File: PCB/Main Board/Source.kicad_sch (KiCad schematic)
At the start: 43 parts, among them K1 G2RL-1, U1 OPA1662

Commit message: minor
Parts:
- added JP? (x2): SolderJumper_2_Bridged, Jumper:SolderJumper-2_P1.3mm_Bridged_RoundedPad1.0x1.5mm, symbol Jumper:SolderJumper_2_Bridged
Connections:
- net Signal: now also JP?.1 (A)
- net at R?.1, U1.6 (-), U1.7: now also JP?.2 (B)
- net at R?.1, U?.1, U?.2 (-): now also JP?.2 (B)
- net at C?.1, JP1.2 (B), R?.2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: now also JP?.1 (A)
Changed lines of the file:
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@@
 	)
 	(junction
+		(at 31.75 104.14)
+		(diameter 0)
+		(color 0 0 0 0)
+	)
+	(junction
+		(at 82.55 53.34)
+		(diameter 0)
+		(color 0 0 0 0)
+	)
+	(junction
 		(at 55.88 101.6)
 		(diameter 0)
@@
 	(wire
 		(pts
+			(xy 31.75 104.14) (xy 36.83 104.14)
+		)
+		(stroke
+			(width 0)
+			(type default)
+		)
+	)
+	(wire
+		(pts
 			(xy 160.02 88.9) (xy 165.1 88.9)
 		)
@@
 	(wire
 		(pts
-			(xy 184.15 133.35) (xy 222.25 133.35)
+			(xy 182.88 133.35) (xy 222.25 133.35)
 		)
 		(stroke
@@
 	(wire
 		(pts
+			(xy 48.26 113.03) (xy 55.88 113.03)
+		)
+		(stroke
+			(width 0)
+			(type default)
+		)
+	)
+	(wire
+		(pts
 			(xy 101.6 140.97) (xy 114.3 140.97)
 		)
@@
 	(wire
 		(pts
-			(xy 31.75 104.14) (xy 36.83 104.14)
+			(xy 29.21 104.14) (xy 31.75 104.14)
 		)
 		(stroke
@@
 	(wire
 		(pts
+			(xy 107.95 62.23) (xy 107.95 50.8)
+		)
+		(stroke
+			(width 0)
+			(type default)
+		)
+	)
+	(wire
+		(pts
 			(xy 241.3 101.6) (xy 250.19 101.6)
 		)
@@
 	(wire
 		(pts
-			(xy 76.2 53.34) (xy 87.63 53.34)
+			(xy 76.2 53.34) (xy 82.55 53.34)
 		)
 		(stroke
@@
 	(wire
 		(pts
-			(xy 201.93 104.14) (xy 184.15 104.14)
+			(xy 100.33 62.23) (xy 107.95 62.23)
+		)
+		(stroke
+			(width 0)
+			(type default)
+		)
+	)
+	(wire
+		(pts
+			(xy 31.75 113.03) (xy 40.64 113.03)
+		)
+		(stroke
+			(width 0)
+			(type default)
+		)
+	)
+	(wire
+		(pts
+			(xy 201.93 104.14) (xy 182.88 104.14)
+		)
+		(stroke
+			(width 0)
+			(type default)
+		)
+	)
+	(wire
+		(pts
+			(xy 55.88 113.03) (xy 55.88 101.6)
 		)
 		(stroke
@@
 	(wire
 		(pts
+			(xy 31.75 113.03) (xy 31.75 104.14)
+		)
+		(stroke
+			(width 0)
+			(type default)
+		)
+	)
+	(wire
+		(pts
 			(xy 82.55 114.3) (xy 82.55 111.76)
 		)
@@
 	(wire
 		(pts
+			(xy 82.55 62.23) (xy 82.55 53.34)
+		)
+		(stroke
+			(width 0)
+			(type default)
+		)
+	)
+	(wire
+		(pts
 			(xy 82.55 48.26) (xy 87.63 48.26)
 		)
@@
 	(wire
 		(pts
+			(xy 92.71 62.23) (xy 82.55 62.23)
+		)
+		(stroke
+			(width 0)
+			(type default)
+		)
+	)
+	(wire
+		(pts
 			(xy 67.31 101.6) (xy 69.85 101.6)
 		)
@@
 	(wire
 		(pts
+			(xy 82.55 53.34) (xy 87.63 53.34)
+		)
+		(stroke
+			(width 0)
+			(type default)
+		)
+	)
+	(wire
+		(pts
 			(xy 66.04 43.18) (xy 63.5 43.18)
 		)
@@
 	(wire
 		(pts
-			(xy 184.15 104.14) (xy 184.15 133.35)
+			(xy 182.88 104.14) (xy 182.88 133.35)
 		)
 		(stroke
@@
 	(hierarchical_label "Signal"
 		(shape input)
-		(at 31.75 104.14 180)
+		(at 29.21 104.14 180)
 		(effects
 			(font
@@
 	)
 	(symbol
+		(lib_id "Jumper:SolderJumper_2_Bridged")
+		(at 44.45 113.03 0)
+		(unit 1)
+		(exclude_from_sim no)
+		(in_bom no)
+		(on_board yes)
+		(dnp no)
+		(property "Reference" "JP?"
+			(at 44.45 109.22 0)
+			(effects
+				(font
+					(size 1.27 1.27)
+				)
+			)
+		)
+		(property "Value" "SolderJumper_2_Bridged"
+			(at 44.45 109.22 0)
+			(effects
+				(font
+					(size 1.27 1.27)
+				)
+				(hide yes)
+			)
+		)
+		(property "Footprint" "Jumper:SolderJumper-2_P1.3mm_Bridged_RoundedPad1.0x1.5mm"
+			(at 44.45 113.03 0)
+			(effects
+				(font
+					(size 1.27 1.27)
+				)
+				(hide yes)
+			)
+		)
+		(property "Datasheet" "~"
+			(at 44.45 113.03 0)
+			(effects
+				(font
+					(size 1.27 1.27)
+				)
+				(hide yes)
+			)
+		)
+		(property "Description" "Solder Jumper, 2-pole, closed/bridged"
+			(at 44.45 113.03 0)
+			(effects
+				(font
+					(size 1.27 1.27)
+				)
+				(hide yes)
+			)
+		)
+		(pin "2"
+		)
+		(pin "1"
+		)
+		(instances
+			(project "Main Board"
+				(path "/20aae4b7-3fb8-4924-82e8-1e7a29a313f8/018dbbaa-4414-4e5b-943a-751bd604c3b0"
+					(reference "JP?")
+					(unit 1)
+				)
+			)
+		)
+	)
+	(symbol
 		(lib_id "Device:C")
 		(at 196.85 114.3 90)
@@
 					(unit 1)
 				)
+			)
+		)
+	)
+	(symbol
+		(lib_id "Jumper:SolderJumper_2_Bridged")
+		(at 96.52 62.23 0)
+		(unit 1)
+		(exclude_from_sim no)
+		(in_bom no)
+		(on_board yes)
+		(dnp no)
+		(property "Reference" "JP?"
+			(at 96.52 58.42 0)
+			(effects
+				(font
+					(size 1.27 1.27)
+				)
+			)
+		)
+		(property "Value" "SolderJumper_2_Bridged"
+			(at 96.52 58.42 0)
+			(effects
+				(font
+					(size 1.27 1.27)
+				)
+				(hide yes)
+			)
+		)
+		(property "Footprint" "Jumper:SolderJumper-2_P1.3mm_Bridged_RoundedPad1.0x1.5mm"
+			(at 96.52 62.23 0)
+			(effects
+				(font
+					(size 1.27 1.27)
+				)
+				(hide yes)
+			)
+		)
+		(property "Datasheet" "~"
+			(at 96.52 62.23 0)
+			(effects
+				(font
+					(size 1.27 1.27)
+				)
+				(hide yes)
+			)
+		)
+		(property "Description" "Solder Jumper, 2-pole, closed/bridged"
+			(at 96.52 62.23 0)
+			(effects
+				(font
+					(size 1.27 1.27)
+				)
+				(hide yes)
+			)
+		)
+		(pin "2"
+		)
+		(pin "1"
+		)
+		(instances
+			(project "Main Board"
+				(path "/20aae4b7-3fb8-4924-82e8-1e7a29a313f8/018dbbaa-4414-4e5b-943a-751bd604c3b0"
+					(reference "JP?")
+					(unit 1)
+				)

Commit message: power supply
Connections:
- net +12V: now reaches K1.A2
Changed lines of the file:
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@@
+	)
+	(symbol
+		(lib_id "power:+12V")
+		(at 261.62 81.28 270)
+		(unit 1)
+		(exclude_from_sim no)
+		(in_bom yes)
+		(on_board yes)
+		(dnp no)
+		(fields_autoplaced yes)
+		(property "Reference" "#PWR044"
+			(at 257.81 81.28 0)
+			(effects
+				(font
+					(size 1.27 1.27)
+				)
+				(hide yes)
+			)
+		)
+		(property "Value" "+12V"
+			(at 265.43 81.2799 90)
+			(effects
+				(font
+					(size 1.27 1.27)
+				)
+				(justify left)
+			)
+		)
+		(property "Footprint" ""
+			(at 261.62 81.28 0)
+			(effects
+				(font
+					(size 1.27 1.27)
+				)
+				(hide yes)
+			)
+		)
+		(property "Datasheet" ""
+			(at 261.62 81.28 0)
+			(effects
+				(font
+					(size 1.27 1.27)
+				)
+				(hide yes)
+			)
+		)
+		(property "Description" "Power symbol creates a global label with name \"+12V\""
+			(at 261.62 81.28 0)
+			(effects
+				(font
+					(size 1.27 1.27)
+				)
+				(hide yes)
+			)
+		)
+		(pin "1"
+		)
+		(instances
+			(project ""
+				(path "/20aae4b7-3fb8-4924-82e8-1e7a29a313f8/018dbbaa-4414-4e5b-943a-751bd604c3b0"
+					(reference "#PWR044")
+					(unit 1)
+				)
+			)
+		)
 	)
 	(symbol

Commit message: Amplifier Switch
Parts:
- removed U1, U? (x5): OPA1662, Package_SO:SOIC-8_3.9x4.9mm_P1.27mm, symbol Device:Opamp_Dual
- added U? (x6): OPA2197xD, Package_SO:SOIC-8_3.9x4.9mm_P1.27mm, symbol Amplifier_Operational:OPA2197xD
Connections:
- net +1.65VA: now also U?.5 (+)
- net +18V: now also U?.8 (V+), U?.8 (V+)
- net -18V: now also U?.4 (V-), U?.4 (V-)
- net Signal: now also U?.5 (+)
- net at C?.2, R?.1, R?.1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: now also U?.1
- net at C?.1, R?.2: now also U?.3 (+)
- net at R?.1, R?.2: now also U?.2 (-)
- net at JP?.2 (B), R?.1, R?.2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: now also U?.6 (-)
- net at JP?.2 (B), R?.1: now also U?.6 (-), U?.7
- net at JP?.2 (B), R?.1: now also U?.1, U?.2 (-)
- net at C?.1, JP1.2 (B), JP?.1 (A)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: now also U?.3 (+)
- net at U?.3 (+): now also U?.7

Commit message: minor
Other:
- added sheet Buffer (buffer.kicad_sch)
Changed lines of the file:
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@@
+		)
+	)
+	(sheet
+		(at 247.65 135.89)
+		(size 12.7 5.08)
+		(exclude_from_sim no)
+		(in_bom yes)
+		(on_board yes)
+		(dnp no)
+		(fields_autoplaced yes)
+		(stroke
+			(width 0.1524)
+			(type solid)
+		)
+		(fill
+			(color 0 0 0 0.0000)
+		)
+		(property "Sheetname" "Buffer"
+			(at 247.65 135.1784 0)
+			(effects
+				(font
+					(size 1.27 1.27)
+				)
+				(justify left bottom)
+			)
+		)
+		(property "Sheetfile" "buffer.kicad_sch"
+			(at 247.65 141.5546 0)
+			(effects
+				(font
+					(size 1.27 1.27)
+				)
+				(justify left top)
+			)
+		)
+		(instances
+			(project "Main Board"
+				(path "/20aae4b7-3fb8-4924-82e8-1e7a29a313f8/018dbbaa-4414-4e5b-943a-751bd604c3b0"
+					(page "9")
+				)
+			)
 		)
 	)

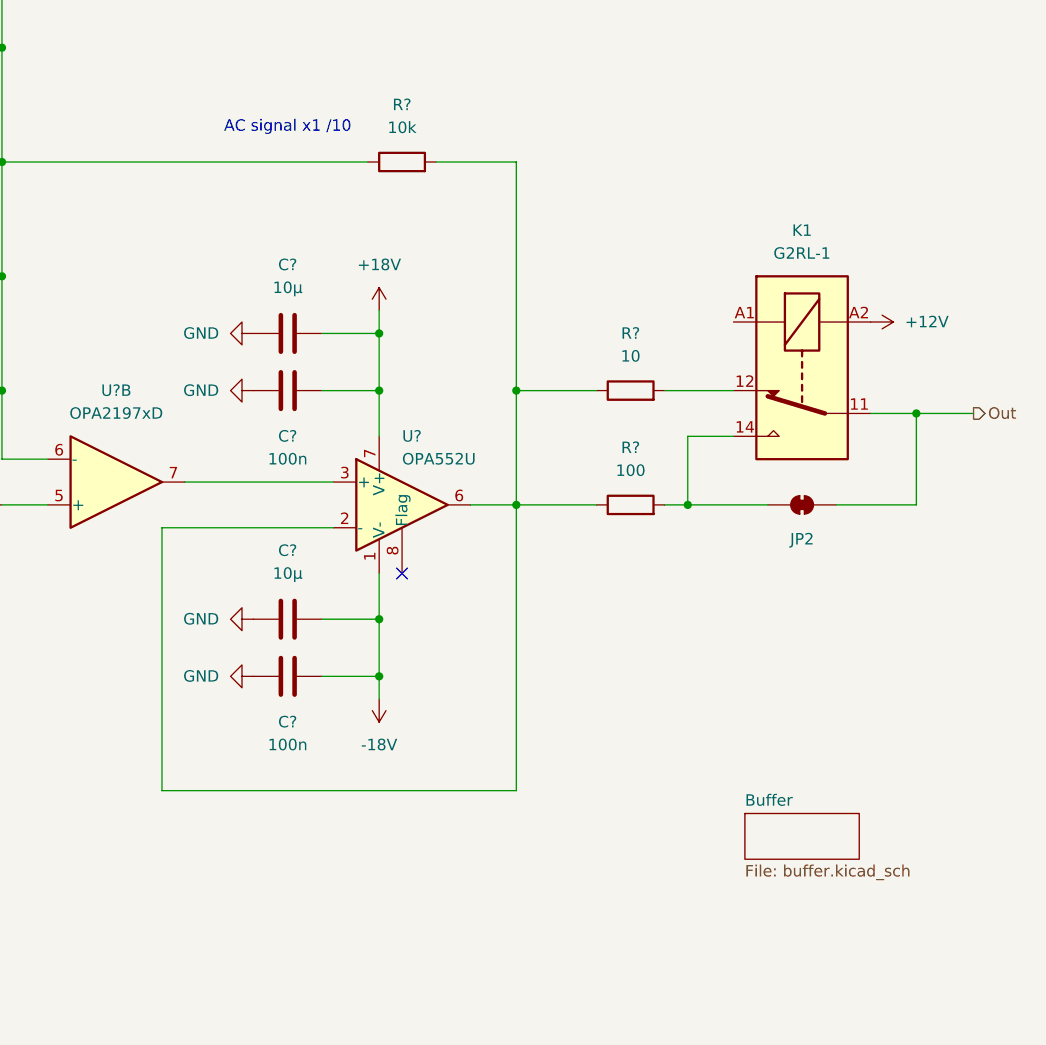
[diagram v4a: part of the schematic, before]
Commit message: created buffer subcircuit
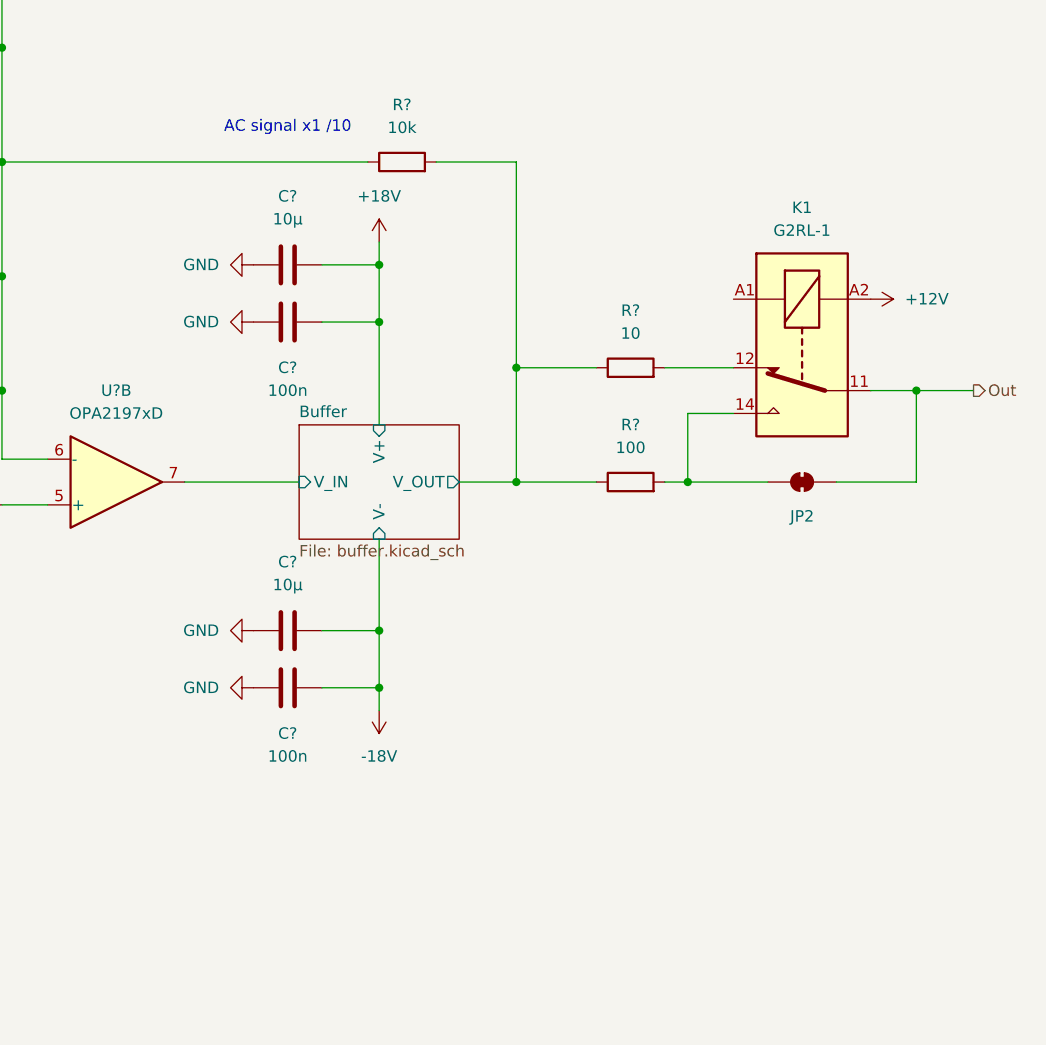
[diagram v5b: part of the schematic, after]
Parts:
- removed U?: OPA552U, Package_SO:SOIC-8_3.9x4.9mm_P1.27mm, symbol Amplifier_Operational:OPA552U
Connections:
- net Buffer/V_OUT: now reaches R?.1, R?.1, R?.2
- net Buffer/V_IN: now reaches U?.7
- no-connect marks 5 -> 4
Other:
- sheet Buffer ports: added  V- , V+, V_IN, V_OUT; removed none
- moved on the sheet: C?, JP2, K1, R?

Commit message: quality of life changes plus wiring plus buffering plus value changes
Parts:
- removed C?: 10µ, symbol Device:C
- removed C?: 100n, symbol Device:C
- added C?: 100n, symbol Device:C
- added C?: 10µ, symbol Device:C
- added D?: BAV199, Package_TO_SOT_SMD:SOT-363_SC-70-6, symbol Diode:BAV99
- added Q?: 2N3906, Package_TO_SOT_THT:TO-92_Inline, symbol Transistor_BJT:2N3906
- added Q?: 2N2219, Package_TO_SOT_THT:TO-39-3, symbol Transistor_BJT:2N2219
- added R? (x2): 2k, symbol Device:R
- added R? (x2): 100m, symbol Device:R
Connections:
- net +18V: now also R?.1, R?.1
- net -18V: now also C?.2, C?.2, R?.2, R?.2
- net GND: now also C?.1, C?.1
- net Buffer/V_IN: no longer names the net of U?.7
- net Buffer/V_IN: now also D?.3 (K)
- net Buffer/V_OUT: no longer names the net of R?.1, R?.1, R?.2
- net Buffer/V_OUT: now also Q?.1 (E), Q?.1 (E)
- new net: D?.1 (K), Q?.2 (B), R?.2
- new net: D?.2 (A), Q?.2 (B), R?.1
- new net: Q?.3 (C), R?.1
- new net: Q?.3 (C), R?.2
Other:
- removed sheet Buffer
- moved on the sheet: C?, JP2, K1, R?

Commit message: footprints and minor
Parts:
- gave numbers to parts that had none: 40
- renumbered JP1 to JP2, JP2 to JP5

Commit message: minor
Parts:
- Q2: value 2N3906 -> 2N4403
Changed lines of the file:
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@@
-	)
-	(symbol
-		(lib_id "Transistor_BJT:2N3906")
-		(at 213.36 107.95 0)
-		(mirror x)
-		(unit 1)
-		(exclude_from_sim no)
-		(in_bom yes)
-		(on_board yes)
-		(dnp no)
-		(property "Reference" "Q2"
-			(at 218.44 109.2201 0)
-			(effects
-				(font
-					(size 1.27 1.27)
-				)
-				(justify left)
-			)
-		)
-		(property "Value" "2N3906"
-			(at 218.44 106.6801 0)
-			(effects
-				(font
-					(size 1.27 1.27)
-				)
-				(justify left)
-			)
-		)
-		(property "Footprint" "Package_TO_SOT_THT:TO-92_Inline"
-			(at 218.44 106.045 0)
-			(effects
-				(font
-					(size 1.27 1.27)
-					(italic yes)
-				)
-				(justify left)
-				(hide yes)
-			)
-		)
-		(property "Datasheet" "https://www.onsemi.com/pub/Collateral/2N3906-D.PDF"
-			(at 213.36 107.95 0)
-			(effects
-				(font
-					(size 1.27 1.27)
-				)
-				(justify left)
-				(hide yes)
-			)
-		)
-		(property "Description" "-0.2A Ic, -40V Vce, Small Signal PNP Transistor, TO-92"
-			(at 213.36 107.95 0)
-			(effects
-				(font
-					(size 1.27 1.27)
-				)
-				(hide yes)
-			)
-		)
-		(pin "1"
-		)
-		(pin "3"
-		)
-		(pin "2"
-		)
-		(instances
-			(project "Main Board"
-				(path "/20aae4b7-3fb8-4924-82e8-1e7a29a313f8/018dbbaa-4414-4e5b-943a-751bd604c3b0"
-					(reference "Q2")
-					(unit 1)
-				)
-			)
-		)
 	)
 	(symbol
@@
 				)
 			)
+		)
+	)
+	(symbol
+		(lib_id "Transistor_BJT:2N3906")
+		(at 213.36 107.95 0)
+		(mirror x)
+		(unit 1)
+		(exclude_from_sim no)
+		(in_bom yes)
+		(on_board yes)
+		(dnp no)
+		(property "Reference" "Q2"
+			(at 218.44 109.2201 0)
+			(effects
+				(font
+					(size 1.27 1.27)
+				)
+				(justify left)
+			)
+		)
+		(property "Value" "2N4403"
+			(at 218.44 106.6801 0)
+			(effects
+				(font
+					(size 1.27 1.27)
+				)
+				(justify left)
+			)
+		)
+		(property "Footprint" "Package_TO_SOT_THT:TO-92_Inline"
+			(at 218.44 106.045 0)
+			(effects
+				(font
+					(size 1.27 1.27)
+					(italic yes)
+				)
+				(justify left)
+				(hide yes)
+			)
+		)
+		(property "Datasheet" "https://www.onsemi.com/pub/Collateral/2N3906-D.PDF"
+			(at 213.36 107.95 0)
+			(effects
+				(font
+					(size 1.27 1.27)
+				)
+				(justify left)
+				(hide yes)
+			)
+		)
+		(property "Description" "-0.2A Ic, -40V Vce, Small Signal PNP Transistor, TO-92"
+			(at 213.36 107.95 0)
+			(effects
+				(font
+					(size 1.27 1.27)
+				)
+				(hide yes)
+			)
+		)
+		(pin "2"
+		)
+		(pin "1"
+		)
+		(pin "3"
+		)
+		(instances
+			(project ""
+				(path "/20aae4b7-3fb8-4924-82e8-1e7a29a313f8/018dbbaa-4414-4e5b-943a-751bd604c3b0"
+					(reference "Q2")
+					(unit 1)
+				)
+			)
